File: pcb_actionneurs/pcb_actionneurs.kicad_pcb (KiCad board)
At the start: 2 copper layers, 74 x 87.5 mm, 50 parts, among them J1 Conn_ST_STDC14, J10 1755736, J11 1755736, J12 1755736, J13 1755736, J14 Conn_01x04, J15 Conn_01x04, J2 USB_C_Receptacle_USB2.0_16P, J3 1755736, J4 1755736, J5 1755736, J6 Conn_02x10_Odd_Even, J7 Conn_01x06, J8 1755736, J9 1755736, K1 Relay_SPDT, K2 Relay_SPDT, K3 Relay_SPDT, U1 STM32G491KEU6, U2 TMC2209_SILENTSTEPSTICK, U3 TMC2209_SILENTSTEPSTICK

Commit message: plein de choses que j'avais pas sauvegardé
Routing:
- net +12V: track 112.4 -> 104.3 mm
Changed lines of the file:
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@@
-	)
-	(segment
-		(start 89.4675 146.5325)
-		(end 91.5 144.5)
-		(width 1)
-		(layer "F.Cu")
-		(net 3)
 	)
 	(segment
@@
 		(width 1)
 		(layer "F.Cu")
-		(net 3)
-	)
-	(segment
-		(start 89.4675 151.8)
-		(end 89.4675 146.5325)
-		(width 1)
-		(layer "F.Cu")

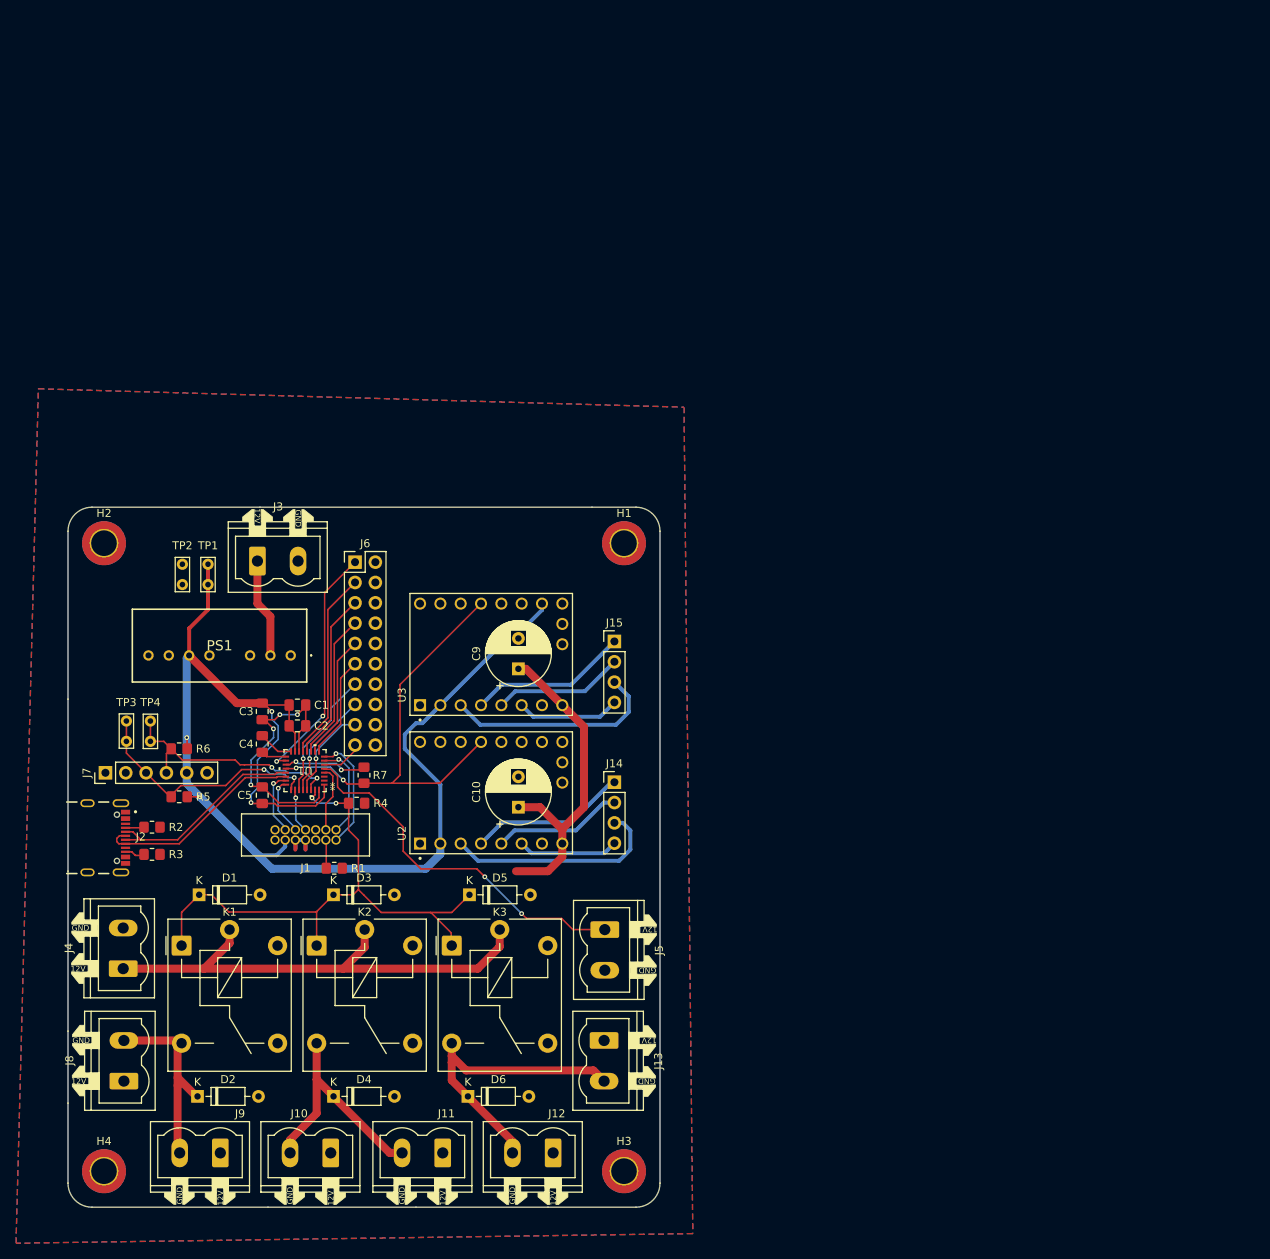
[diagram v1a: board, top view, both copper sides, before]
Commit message: Ajout BAU servo PAMI, finitions PCB Actionneurs, fichier fab stencil. Version commandée PAMI & Actionneurs
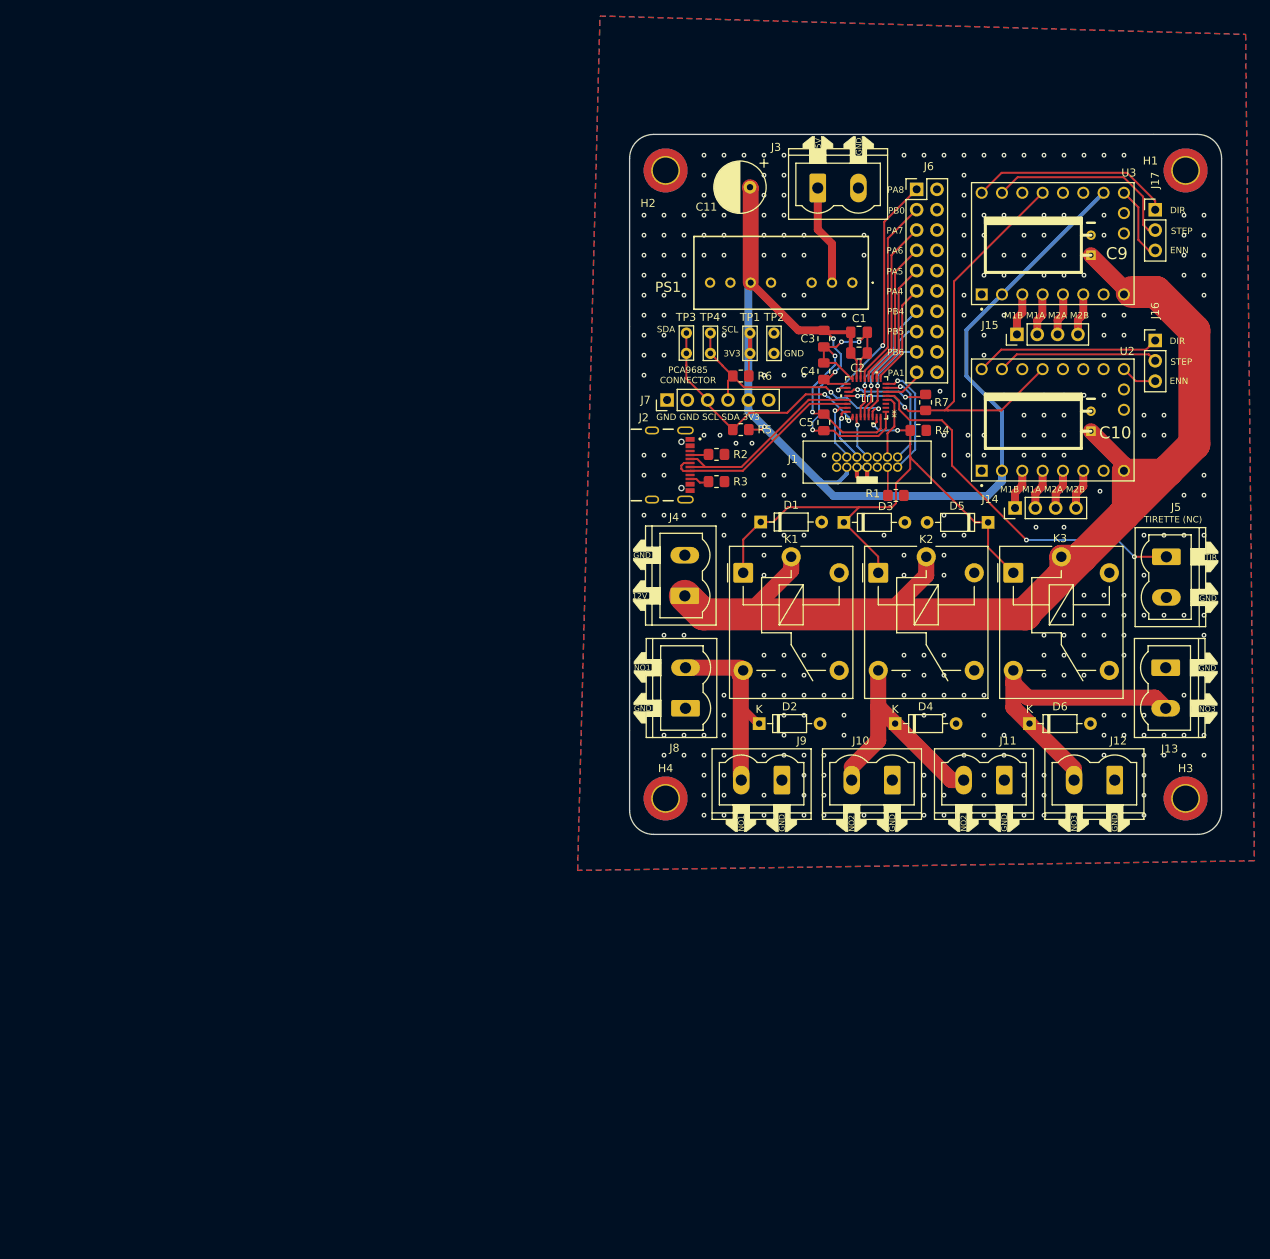
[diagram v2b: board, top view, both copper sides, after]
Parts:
- added C11: 100uF, Capacitor_THT:C_Radial_D6.3mm_H11.0mm_P2.50mm, F.Cu at (120.8, 59.0)
- added G***: LOGO, Modelec:logo_modelec, B.Cu at (159.0, 113.0)
- added J16: Conn_01x03, Connector_PinHeader_2.54mm:PinHeader_1x03_P2.54mm_Vertical, F.Cu at (171.4, 78.2)
- added J17: Conn_01x03, Connector_PinHeader_2.54mm:PinHeader_1x03_P2.54mm_Vertical, F.Cu at (171.4, 61.8)
- C10, C9: value 100uF 50V -> 100uF 16V; footprint Capacitor_THT:CP_Radial_D8.0mm_P3.80mm -> w_capacitors:CP_6.3x11mm_horiz-L
- moved C9 89.0 mm to (163.4, 66.2), turned to 0 degrees
- moved U3 87.0 mm to (158.6, 66.0)
- moved C10 86.3 mm to (163.4, 88.2), turned to 0 degrees
- moved TP3 85.2 mm to (112.8, 77.2)
- moved TP4 85.2 mm to (115.8, 79.8)
- moved R3 84.6 mm to (116.6, 95.8)
- moved J2 84.6 mm to (108.5, 93.7)
- moved R2 84.6 mm to (116.6, 92.4)
- moved D2 84.3 mm to (121.9, 126.0)
- moved D6 84.3 mm to (155.7, 126.0)
- moved J1 84.3 mm to (131.6, 92.7)
- moved J5 84.3 mm to (172.8, 105.2)
- moved J6 84.3 mm to (141.6, 59.3)
- moved J8 84.3 mm to (112.7, 124.1)
- moved K2 84.3 mm to (136.8, 107.2)
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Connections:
- net Net-(J6-Pin_1) renamed /PA8
- net Net-(J6-Pin_11) renamed /PA4
- net Net-(J6-Pin_13) renamed /PB4
- net Net-(J6-Pin_15) renamed /PB5
- net Net-(J6-Pin_17) renamed /PB6
- net Net-(J6-Pin_19) renamed /PA1
- net Net-(J6-Pin_3) renamed /PB0
- net Net-(J6-Pin_5) renamed /PA7
- net Net-(J6-Pin_7) renamed /PA6
- net Net-(J6-Pin_9) renamed /PA5
- J2 pad SH1: (no net) -> GND
- J2 pad SH2: (no net) -> GND
- J2 pad SH3: (no net) -> GND
- J2 pad SH4: (no net) -> GND
- U2 pad 10: unconnected-(U2-STEP-Pad10) -> Net-(J16-Pin_2)
- U2 pad 14: unconnected-(U2-MS2-Pad14) -> GND
- U2 pad 15: unconnected-(U2-MS1-Pad15) -> GND
- U2 pad 16: unconnected-(U2-~{EN}-Pad16) -> Net-(J16-Pin_3)
- U2 pad 3: Net-(J14-Pin_3) -> Net-(J14-Pin_1)
- U2 pad 4: Net-(J14-Pin_1) -> Net-(J14-Pin_2)
- U2 pad 5: Net-(J14-Pin_2) -> Net-(J14-Pin_3)
- U2 pad 9: unconnected-(U2-DIR-Pad9) -> Net-(J16-Pin_1)
- U3 pad 10: unconnected-(U3-STEP-Pad10) -> Net-(J17-Pin_2)
- U3 pad 14: unconnected-(U3-MS2-Pad14) -> GND
- U3 pad 16: unconnected-(U3-~{EN}-Pad16) -> Net-(J17-Pin_3)
- U3 pad 3: Net-(J15-Pin_3) -> Net-(J15-Pin_1)
- U3 pad 4: Net-(J15-Pin_1) -> Net-(J15-Pin_2)
- U3 pad 5: Net-(J15-Pin_2) -> Net-(J15-Pin_3)
- U3 pad 9: unconnected-(U3-DIR-Pad9) -> Net-(J17-Pin_1)
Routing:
- net +12V: track 104.3 -> 144.1 mm
- net Net-(J17-Pin_1): track 0.00 -> 25.3 mm
- net Net-(J17-Pin_2): track 0.00 -> 24.7 mm
- net Net-(J16-Pin_1): track 0.00 -> 23.2 mm
- net Net-(J14-Pin_3): track 27.5 -> 5.03 mm
- net Net-(J15-Pin_3): track 27.2 -> 5.30 mm
- net Net-(J16-Pin_2): track 0.00 -> 20.5 mm
- net Net-(J14-Pin_1): track 19.8 -> 5.03 mm
- net Net-(J15-Pin_1): track 20.0 -> 5.28 mm
- net Net-(J14-Pin_2): track 16.3 -> 5.03 mm
- net Net-(J15-Pin_2): track 16.4 -> 5.28 mm
- net +3V3: track 165.8 -> 175.5 mm
- net Net-(J17-Pin_3): track 0.00 -> 9.29 mm
- net Net-(J15-Pin_4): track 12.9 -> 5.28 mm
- net Net-(J14-Pin_4): track 12.6 -> 5.03 mm
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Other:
- board text added: "3V3"
- board text added: "C11"
- board text added: "Carte actionneurs V1 Modelec ISEN 2025"
- board text added: "DIR"
- board text added: "ENN"
- board text added: "GND"
- board text added: "GND GND SCL SDA 3V3"
- board text added: "M1B M1A M2A M2B"
- board text added: "PA1"
- board text added: "PA4"
- board text added: "PA5"
- board text added: "PA6"
- board text added: "PA7"
- board text added: "PA8"
- board text added: "PB0"
- board text added: "PB4"
- board text added: "PB5"
- board text added: "PB6"
- board text added: "PCA9685 CONNECTOR"
- board text added: "SCL"
- board text added: "SDA"
- board text added: "STEP"
- board text added: "TIRETTE (NC)"
